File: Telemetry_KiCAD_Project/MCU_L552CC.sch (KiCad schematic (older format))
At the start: 13 parts

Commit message: Annotated Components
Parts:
- gave numbers to parts that had none: 13
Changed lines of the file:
@@
 $EndDescr
 $Comp
-L RDT_Custom_Symbols:STM32L552CCU U?
+L RDT_Custom_Symbols:STM32L552CCU U5
 U 1 1 619FC25F
 P 6000 1800
-F 0 "U?" H 6150 2100 50  0000 C CNN
+F 0 "U5" H 6150 2100 50  0000 C CNN
 F 1 "STM32L552CCU" H 6150 2000 50  0000 C CNN
 F 2 "Package_QFP:LQFP-48_7x7mm_P0.5mm" H 6000 1800 50  0001 C CNN
@@
 $EndComp
 $Comp
-L power:+3.3V #PWR?
+L power:+3.3V #PWR0131
 U 1 1 619FD913
 P 6600 1700
-F 0 "#PWR?" H 6600 1550 50  0001 C CNN
+F 0 "#PWR0131" H 6600 1550 50  0001 C CNN
 F 1 "+3.3V" H 6615 1873 50  0000 C CNN
 F 2 "" H 6600 1700 50  0001 C CNN
@@
 USB_DM
 $Comp
-L power:GND #PWR?
+L power:GND #PWR0132
 U 1 1 61A048CD
 P 6050 5050
-F 0 "#PWR?" H 6050 4800 50  0001 C CNN
+F 0 "#PWR0132" H 6050 4800 50  0001 C CNN
 F 1 "GND" H 6055 4877 50  0000 C CNN
 F 2 "" H 6050 5050 50  0001 C CNN
@@
 	4400 2900 4400 2800
 $Comp
-L Device:C_Small C?
+L Device:C_Small C25
 U 1 1 61A0011F
 P 4400 3000
-F 0 "C?" H 4492 3046 50  0000 L CNN
+F 0 "C25" H 4492 3046 50  0000 L CNN
 F 1 "30pF" H 4492 2955 50  0000 L CNN
 F 2 "" H 4400 3000 50  0001 C CNN
@@
 $EndComp
 $Comp
-L power:GND #PWR?
+L power:GND #PWR0133
 U 1 1 61A00A06
 P 4800 3100
-F 0 "#PWR?" H 4800 2850 50  0001 C CNN
+F 0 "#PWR0133" H 4800 2850 50  0001 C CNN
 F 1 "GND" H 4805 2927 50  0000 C CNN
 F 2 "" H 4800 3100 50  0001 C CNN
@@
 $EndComp
 $Comp
-L power:GND #PWR?
+L power:GND #PWR0134
 U 1 1 61A0071A
 P 4400 3100
-F 0 "#PWR?" H 4400 2850 50  0001 C CNN
+F 0 "#PWR0134" H 4400 2850 50  0001 C CNN
 F 1 "GND" H 4405 2927 50  0000 C CNN
 F 2 "" H 4400 3100 50  0001 C CNN
@@
 $EndComp
 $Comp
-L Device:C_Small C?
+L Device:C_Small C26
 U 1 1 61A00503
 P 4800 3000
-F 0 "C?" H 4892 3046 50  0000 L CNN
+F 0 "C26" H 4892 3046 50  0000 L CNN
 F 1 "30pF" H 4892 2955 50  0000 L CNN
 F 2 "" H 4800 3000 50  0001 C CNN
@@
 $EndComp
 $Comp
-L Device:Crystal_Small Y?
+L Device:Crystal_Small Y3
 U 1 1 619FF2E0
 P 4600 2800
-F 0 "Y?" H 4600 3025 50  0000 C CNN
+F 0 "Y3" H 4600 3025 50  0000 C CNN
 F 1 "32MHz" H 4600 2934 50  0000 C CNN
 F 2 "" H 4600 2800 50  0001 C CNN
@@
 	4050 2300 4050 2250
 $Comp
-L power:GND #PWR?
+L power:GND #PWR0135
 U 1 1 619FE786
 P 4050 2300
-F 0 "#PWR?" H 4050 2050 50  0001 C CNN
+F 0 "#PWR0135" H 4050 2050 50  0001 C CNN
 F 1 "GND" H 4055 2127 50  0000 C CNN
 F 2 "" H 4050 2300 50  0001 C CNN
@@
 Microcontroller\nInput Power Filtering
 $Comp
-L power:+3.3V #PWR?
+L power:+3.3V #PWR0136
 U 1 1 61A127A6
 P 900 1450
-F 0 "#PWR?" H 900 1300 50  0001 C CNN
+F 0 "#PWR0136" H 900 1300 50  0001 C CNN
 F 1 "+3.3V" H 915 1623 50  0000 C CNN
 F 2 "" H 900 1450 50  0001 C CNN
@@
 $EndComp
 $Comp
-L Device:C_Small C?
+L Device:C_Small C20
 U 1 1 61A12B2B
 P 900 1650
-F 0 "C?" H 992 1696 50  0000 L CNN
+F 0 "C20" H 992 1696 50  0000 L CNN
 F 1 "1uF" H 992 1605 50  0000 L CNN
 F 2 "" H 900 1650 50  0001 C CNN
@@
 $EndComp
 $Comp
-L Device:C_Small C?
+L Device:C_Small C21
 U 1 1 61A13102
 P 1300 1650
-F 0 "C?" H 1392 1696 50  0000 L CNN
+F 0 "C21" H 1392 1696 50  0000 L CNN
 F 1 "100nF" H 1392 1605 50  0000 L CNN
 F 2 "" H 1300 1650 50  0001 C CNN
@@
 $EndComp
 $Comp
-L Device:C_Small C?
+L Device:C_Small C22
 U 1 1 61A13DFC
 P 1750 1650
-F 0 "C?" H 1842 1696 50  0000 L CNN
+F 0 "C22" H 1842 1696 50  0000 L CNN
 F 1 "100nF" H 1842 1605 50  0000 L CNN
 F 2 "" H 1750 1650 50  0001 C CNN
@@
 $EndComp
 $Comp
-L Device:C_Small C?
+L Device:C_Small C23
 U 1 1 61A13E02
 P 2200 1650
-F 0 "C?" H 2292 1696 50  0000 L CNN
+F 0 "C23" H 2292 1696 50  0000 L CNN
 F 1 "100nF" H 2292 1605 50  0000 L CNN
 F 2 "" H 2200 1650 50  0001 C CNN
@@
 $EndComp
 $Comp
-L Device:C_Small C?
+L Device:C_Small C24
 U 1 1 61A142DA
 P 2650 1650
-F 0 "C?" H 2742 1696 50  0000 L CNN
+F 0 "C24" H 2742 1696 50  0000 L CNN
 F 1 "100nF" H 2742 1605 50  0000 L CNN
 F 2 "" H 2650 1650 50  0001 C CNN
@@
 $EndComp
 $Comp
-L power:GND #PWR?
+L power:GND #PWR0137
 U 1 1 61A159EE
 P 900 1850
-F 0 "#PWR?" H 900 1600 50  0001 C CNN
+F 0 "#PWR0137" H 900 1600 50  0001 C CNN
 F 1 "GND" H 905 1677 50  0000 C CNN
 F 2 "" H 900 1850 50  0001 C CNN
@@
 PVD_IN is the Power Voltage Dropout pin,\nused to detect and respond to brownout conditions.
 $Comp
-L power:+3.3V #PWR?
+L power:+3.3V #PWR0138
 U 1 1 61A1E3D8
 P 900 3350
-F 0 "#PWR?" H 900 3200 50  0001 C CNN
+F 0 "#PWR0138" H 900 3200 50  0001 C CNN
 F 1 "+3.3V" H 915 3523 50  0000 C CNN
 F 2 "" H 900 3350 50  0001 C CNN
@@
 $EndComp
 $Comp
-L Device:R_Small R?
+L Device:R_Small R3
 U 1 1 61A1EA19
 P 1100 3600
-F 0 "R?" V 904 3600 50  0000 C CNN
+F 0 "R3" V 904 3600 50  0000 C CNN
 F 1 "4.7k" V 995 3600 50  0000 C CNN
 F 2 "" H 1100 3600 50  0001 C CNN
@@
 	900  3600 1000 3600
 $Comp
-L Device:R_Small R?
+L Device:R_Small R4
 U 1 1 61A20049
 P 1100 3900
-F 0 "R?" V 904 3900 50  0000 C CNN
+F 0 "R4" V 904 3900 50  0000 C CNN
 F 1 "4.7k" V 995 3900 50  0000 C CNN
 F 2 "" H 1100 3900 50  0001 C CNN
@@
 Text HLabel 1200 3900 2    50   Input ~ 0
 I2C1_SDA
-$Comp
-L power:+3.3V #PWR?
-U 1 1 61A22B89
-P 900 4500
-F 0 "#PWR?" H 900 4350 50  0001 C CNN
-F 1 "+3.3V" H 915 4673 50  0000 C CNN
-F 2 "" H 900 4500 50  0001 C CNN
-F 3 "" H 900 4500 50  0001 C CNN
-	1    900  4500
-	1    0    0    -1
-$EndComp
-$Comp
-L Device:R_Small R?
-U 1 1 61A22B8F
-P 1100 4750
-F 0 "R?" V 904 4750 50  0000 C CNN
-F 1 "4.7k" V 995 4750 50  0000 C CNN
-F 2 "" H 1100 4750 50  0001 C CNN
-F 3 "~" H 1100 4750 50  0001 C CNN
-	1    1100 4750
-	0    1    1    0
-$EndComp
-Wire Wire Line
-	900  4500 900  4750
-Wire Wire Line
-	900  4750 1000 4750
-$Comp
-L Device:R_Small R?
-U 1 1 61A22B97
-P 1100 5050
-F 0 "R?" V 904 5050 50  0000 C CNN
-F 1 "4.7k" V 995 5050 50  0000 C CNN
-F 2 "" H 1100 5050 50  0001 C CNN
-F 3 "~" H 1100 5050 50  0001 C CNN
-	1    1100 5050
-	0    1    1    0
-$EndComp
-Wire Wire Line
-	1000 5050 900  5050
-Wire Wire Line
-	900  5050 900  4750
-Connection ~ 900  4750
-Text HLabel 1200 4750 2    50   Input ~ 0
-I2C1_SCL
-Text HLabel 1200 5050 2    50   Input ~ 0
-I2C1_SDA
 Text Notes 850  3050 0    50   ~ 0
 I2C1 Pullup Resistors
-Text Notes 850  4200 0    50   ~ 0
-I2C1 Pullup Resistors
 Wire Notes Line
 	750  3100 1700 3100
@@
 Wire Notes Line
 	750  4000 750  3100
-Wire Notes Line
-	750  4250 1700 4250
-Wire Notes Line
-	1700 4250 1700 5150
-Wire Notes Line
-	1700 5150 750  5150
-Wire Notes Line
-	750  5150 750  4250
 Wire Notes Line
 	7500 1400 7500 5350
@@
 Wire Notes Line
 	750  1200 750  2100
+Wire Notes Line
+	750  5150 750  4250
+Wire Notes Line
+	1700 5150 750  5150
+Wire Notes Line
+	1700 4250 1700 5150
+Wire Notes Line
+	750  4250 1700 4250
+Text Notes 850  4200 0    50   ~ 0
+I2C1 Pullup Resistors
+Text HLabel 1200 5050 2    50   Input ~ 0
+I2C1_SDA
+Text HLabel 1200 4750 2    50   Input ~ 0
+I2C1_SCL
+Wire Wire Line
+	900  5050 900  4750
+Wire Wire Line
+	1000 5050 900  5050
+$Comp
+L Device:R_Small R6
+U 1 1 61A22B97
+P 1100 5050
+F 0 "R6" V 904 5050 50  0000 C CNN
+F 1 "4.7k" V 995 5050 50  0000 C CNN
+F 2 "" H 1100 5050 50  0001 C CNN
+F 3 "~" H 1100 5050 50  0001 C CNN
+	1    1100 5050
+	0    1    1    0
+$EndComp
+Wire Wire Line
+	900  4750 1000 4750
+Connection ~ 900  4750
+Wire Wire Line
+	900  4500 900  4750
+$Comp
+L Device:R_Small R5
+U 1 1 61A22B8F
+P 1100 4750
+F 0 "R5" V 904 4750 50  0000 C CNN
+F 1 "4.7k" V 995 4750 50  0000 C CNN
+F 2 "" H 1100 4750 50  0001 C CNN
+F 3 "~" H 1100 4750 50  0001 C CNN
+	1    1100 4750
+	0    1    1    0
+$EndComp
+$Comp
+L power:+3.3V #PWR0139
+U 1 1 61A22B89
+P 900 4500
+F 0 "#PWR0139" H 900 4350 50  0001 C CNN
+F 1 "+3.3V" H 915 4673 50  0000 C CNN
+F 2 "" H 900 4500 50  0001 C CNN
+F 3 "" H 900 4500 50  0001 C CNN
+	1    900  4500
+	1    0    0    -1
+$EndComp
 $EndSCHEMATC

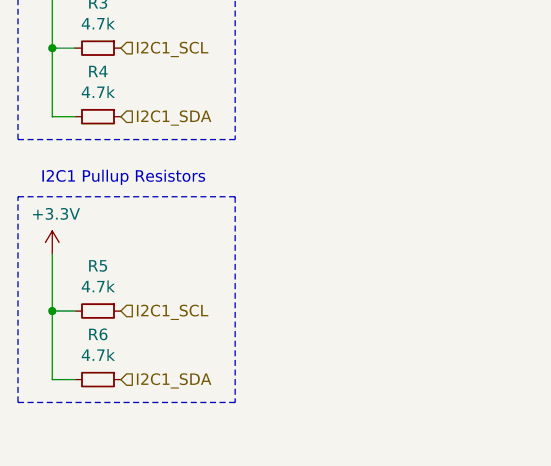
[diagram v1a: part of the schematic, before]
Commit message: I2C2 removed from MCU
Carry over from copying the file from the Data Collection board
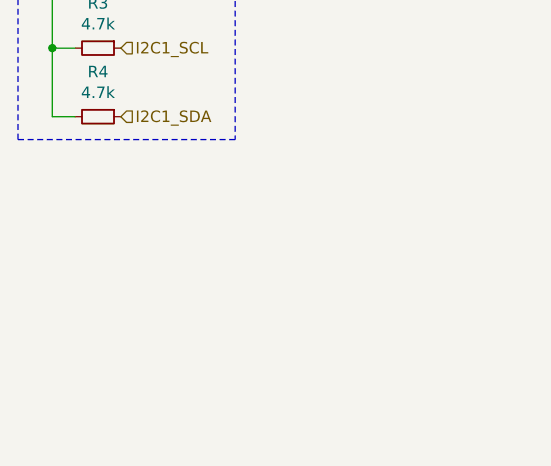
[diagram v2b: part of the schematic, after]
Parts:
- removed R5, R6: 4.7k, symbol Device:R_Small
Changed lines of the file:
@@
 Wire Notes Line
 	750  1200 750  2100
-Wire Notes Line
-	750  5150 750  4250
-Wire Notes Line
-	1700 5150 750  5150
-Wire Notes Line
-	1700 4250 1700 5150
-Wire Notes Line
-	750  4250 1700 4250
-Text Notes 850  4200 0    50   ~ 0
-I2C1 Pullup Resistors
-Text HLabel 1200 5050 2    50   Input ~ 0
-I2C1_SDA
-Text HLabel 1200 4750 2    50   Input ~ 0
-I2C1_SCL
-Wire Wire Line
-	900  5050 900  4750
-Wire Wire Line
-	1000 5050 900  5050
-$Comp
-L Device:R_Small R6
-U 1 1 61A22B97
-P 1100 5050
-F 0 "R6" V 904 5050 50  0000 C CNN
-F 1 "4.7k" V 995 5050 50  0000 C CNN
-F 2 "" H 1100 5050 50  0001 C CNN
-F 3 "~" H 1100 5050 50  0001 C CNN
-	1    1100 5050
-	0    1    1    0
-$EndComp
-Wire Wire Line
-	900  4750 1000 4750
-Connection ~ 900  4750
-Wire Wire Line
-	900  4500 900  4750
-$Comp
-L Device:R_Small R5
-U 1 1 61A22B8F
-P 1100 4750
-F 0 "R5" V 904 4750 50  0000 C CNN
-F 1 "4.7k" V 995 4750 50  0000 C CNN
-F 2 "" H 1100 4750 50  0001 C CNN
-F 3 "~" H 1100 4750 50  0001 C CNN
-	1    1100 4750
-	0    1    1    0
-$EndComp
-$Comp
-L power:+3.3V #PWR0139
-U 1 1 61A22B89
-P 900 4500
-F 0 "#PWR0139" H 900 4350 50  0001 C CNN
-F 1 "+3.3V" H 915 4673 50  0000 C CNN
-F 2 "" H 900 4500 50  0001 C CNN
-F 3 "" H 900 4500 50  0001 C CNN
-	1    900  4500
-	1    0    0    -1
-$EndComp
 $EndSCHEMATC

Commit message: Corrected hierarchical pin directions, squashed bugs
There are still some warnings about pins being connected but not driven, don't know how to fix those at the moment
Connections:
- no-connect marks 0 -> 14
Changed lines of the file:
@@
 Text HLabel 5550 2050 0    50   Input ~ 0
 NRST
-Text HLabel 6750 3350 2    50   Input ~ 0
+Text HLabel 6750 3350 2    50   Output ~ 0
 SPI1_SCK
 Text HLabel 6750 3850 2    50   Input ~ 0
 SPI1_MISO
-Text HLabel 6750 3950 2    50   Input ~ 0
+Text HLabel 6750 3950 2    50   Output ~ 0
 SPI1_MOSI
-Text HLabel 5550 4250 0    50   Input ~ 0
+Text HLabel 5550 4250 0    50   Output ~ 0
 SPI2_SCK
 Text HLabel 5550 4650 0    50   Input ~ 0
 SPI2_MISO
-Text HLabel 5550 4750 0    50   Input ~ 0
+Text HLabel 5550 4750 0    50   Output ~ 0
 SPI2_MOSI
-Text HLabel 6750 4550 2    50   Input ~ 0
+Text HLabel 6750 4550 2    50   BiDi ~ 0
 DEBUG_SWDIO
-Text HLabel 5550 4150 0    50   Input ~ 0
-I2C1_SDA
-Text HLabel 5550 3850 0    50   Input ~ 0
+Text HLabel 5550 3850 0    50   BiDi ~ 0
 I2C1_SCL
-Text HLabel 5550 3750 0    50   Input ~ 0
+Text HLabel 5550 3750 0    50   Output ~ 0
 SPI3_MOSI
 Text HLabel 5550 3650 0    50   Input ~ 0
 SPI3_MISO
-Text HLabel 5550 3550 0    50   Input ~ 0
-SPI3_SCK
 Text HLabel 6750 4650 2    50   Input ~ 0
 DEBUG_SWCLK
-Text HLabel 6750 4450 2    50   Input ~ 0
+Text HLabel 6750 4450 2    50   BiDi ~ 0
 USB_DP
-Text HLabel 6750 4350 2    50   Input ~ 0
+Text HLabel 6750 4350 2    50   BiDi ~ 0
 USB_DM
 $Comp
@@
 Wire Wire Line
 	4800 2550 5550 2550
-Text HLabel 5550 3950 0    50   Input ~ 0
+Text HLabel 5550 3950 0    50   BiDi ~ 0
 I2C1_EN
 Text Notes 750  1000 0    100  ~ 0
@@
 Text HLabel 5550 4550 0    50   Input ~ 0
 EXT_INT2
-Text HLabel 6750 3750 2    50   Input ~ 0
+Text HLabel 6750 3750 2    50   Output ~ 0
 ABORT_2
-Text HLabel 6750 3550 2    50   Input ~ 0
+Text HLabel 6750 3550 2    50   Output ~ 0
 ABORT_1
-Text HLabel 5550 4450 0    50   Input ~ 0
+Text HLabel 5550 4450 0    50   Output ~ 0
 ~SPI2_CS
-Text HLabel 6750 3650 2    50   Input ~ 0
+Text HLabel 6750 3650 2    50   Output ~ 0
 ~SPI3_CS
 Wire Notes Line
@@
 Wire Notes Line
 	750  1200 750  2100
+NoConn ~ 5550 2750
+NoConn ~ 5550 2850
+NoConn ~ 5550 2950
+NoConn ~ 5550 3050
+NoConn ~ 5550 3350
+NoConn ~ 5550 3450
+NoConn ~ 5550 4050
+NoConn ~ 5550 4350
+NoConn ~ 6750 4750
+NoConn ~ 6750 4250
+NoConn ~ 6750 4150
+NoConn ~ 6750 4050
+NoConn ~ 6750 3450
+NoConn ~ 6750 3250
+Text HLabel 5550 3550 0    50   Output ~ 0
+SPI3_SCK
+Text HLabel 5550 4150 0    50   BiDi ~ 0
+I2C1_SDA
 $EndSCHEMATC

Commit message: Assigned footprints to all components (except duplexer)
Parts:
- C20, C21, C22, C23, C24, C25, C26: footprint (none) -> Capacitor_SMD:C_0603_1608Metric
- R3, R4: footprint (none) -> Resistor_SMD:R_0201_0603Metric
- Y3: footprint (none) -> Crystal:Crystal_SMD_0603-2Pin_6.0x3.5mm
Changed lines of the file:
@@
 F 0 "C25" H 4492 3046 50  0000 L CNN
 F 1 "30pF" H 4492 2955 50  0000 L CNN
-F 2 "" H 4400 3000 50  0001 C CNN
+F 2 "Capacitor_SMD:C_0603_1608Metric" H 4400 3000 50  0001 C CNN
 F 3 "~" H 4400 3000 50  0001 C CNN
 	1    4400 3000
@@
 F 0 "C26" H 4892 3046 50  0000 L CNN
 F 1 "30pF" H 4892 2955 50  0000 L CNN
-F 2 "" H 4800 3000 50  0001 C CNN
+F 2 "Capacitor_SMD:C_0603_1608Metric" H 4800 3000 50  0001 C CNN
 F 3 "~" H 4800 3000 50  0001 C CNN
 	1    4800 3000
@@
 F 0 "Y3" H 4600 3025 50  0000 C CNN
 F 1 "32MHz" H 4600 2934 50  0000 C CNN
-F 2 "" H 4600 2800 50  0001 C CNN
+F 2 "Crystal:Crystal_SMD_0603-2Pin_6.0x3.5mm" H 4600 2800 50  0001 C CNN
 F 3 "~" H 4600 2800 50  0001 C CNN
 	1    4600 2800
@@
 F 0 "C20" H 992 1696 50  0000 L CNN
 F 1 "1uF" H 992 1605 50  0000 L CNN
-F 2 "" H 900 1650 50  0001 C CNN
+F 2 "Capacitor_SMD:C_0603_1608Metric" H 900 1650 50  0001 C CNN
 F 3 "~" H 900 1650 50  0001 C CNN
 	1    900  1650
@@
 F 0 "C21" H 1392 1696 50  0000 L CNN
 F 1 "100nF" H 1392 1605 50  0000 L CNN
-F 2 "" H 1300 1650 50  0001 C CNN
+F 2 "Capacitor_SMD:C_0603_1608Metric" H 1300 1650 50  0001 C CNN
 F 3 "~" H 1300 1650 50  0001 C CNN
 	1    1300 1650
@@
 F 0 "C22" H 1842 1696 50  0000 L CNN
 F 1 "100nF" H 1842 1605 50  0000 L CNN
-F 2 "" H 1750 1650 50  0001 C CNN
+F 2 "Capacitor_SMD:C_0603_1608Metric" H 1750 1650 50  0001 C CNN
 F 3 "~" H 1750 1650 50  0001 C CNN
 	1    1750 1650
@@
 F 0 "C23" H 2292 1696 50  0000 L CNN
 F 1 "100nF" H 2292 1605 50  0000 L CNN
-F 2 "" H 2200 1650 50  0001 C CNN
+F 2 "Capacitor_SMD:C_0603_1608Metric" H 2200 1650 50  0001 C CNN
 F 3 "~" H 2200 1650 50  0001 C CNN
 	1    2200 1650
@@
 F 0 "C24" H 2742 1696 50  0000 L CNN
 F 1 "100nF" H 2742 1605 50  0000 L CNN
-F 2 "" H 2650 1650 50  0001 C CNN
+F 2 "Capacitor_SMD:C_0603_1608Metric" H 2650 1650 50  0001 C CNN
 F 3 "~" H 2650 1650 50  0001 C CNN
 	1    2650 1650
@@
 F 0 "R3" V 904 3600 50  0000 C CNN
 F 1 "4.7k" V 995 3600 50  0000 C CNN
-F 2 "" H 1100 3600 50  0001 C CNN
+F 2 "Resistor_SMD:R_0201_0603Metric" H 1100 3600 50  0001 C CNN
 F 3 "~" H 1100 3600 50  0001 C CNN
 	1    1100 3600
@@
 F 0 "R4" V 904 3900 50  0000 C CNN
 F 1 "4.7k" V 995 3900 50  0000 C CNN
-F 2 "" H 1100 3900 50  0001 C CNN
+F 2 "Resistor_SMD:R_0201_0603Metric" H 1100 3900 50  0001 C CNN
 F 3 "~" H 1100 3900 50  0001 C CNN
 	1    1100 3900
